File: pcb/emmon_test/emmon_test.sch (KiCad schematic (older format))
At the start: 11 parts, among them J1 Conn_01x06_Female, J2 Conn_01x08_Female, J3 Conn_01x15_Female, J4 Conn_01x15_Female, J5 Conn_01x04_Female

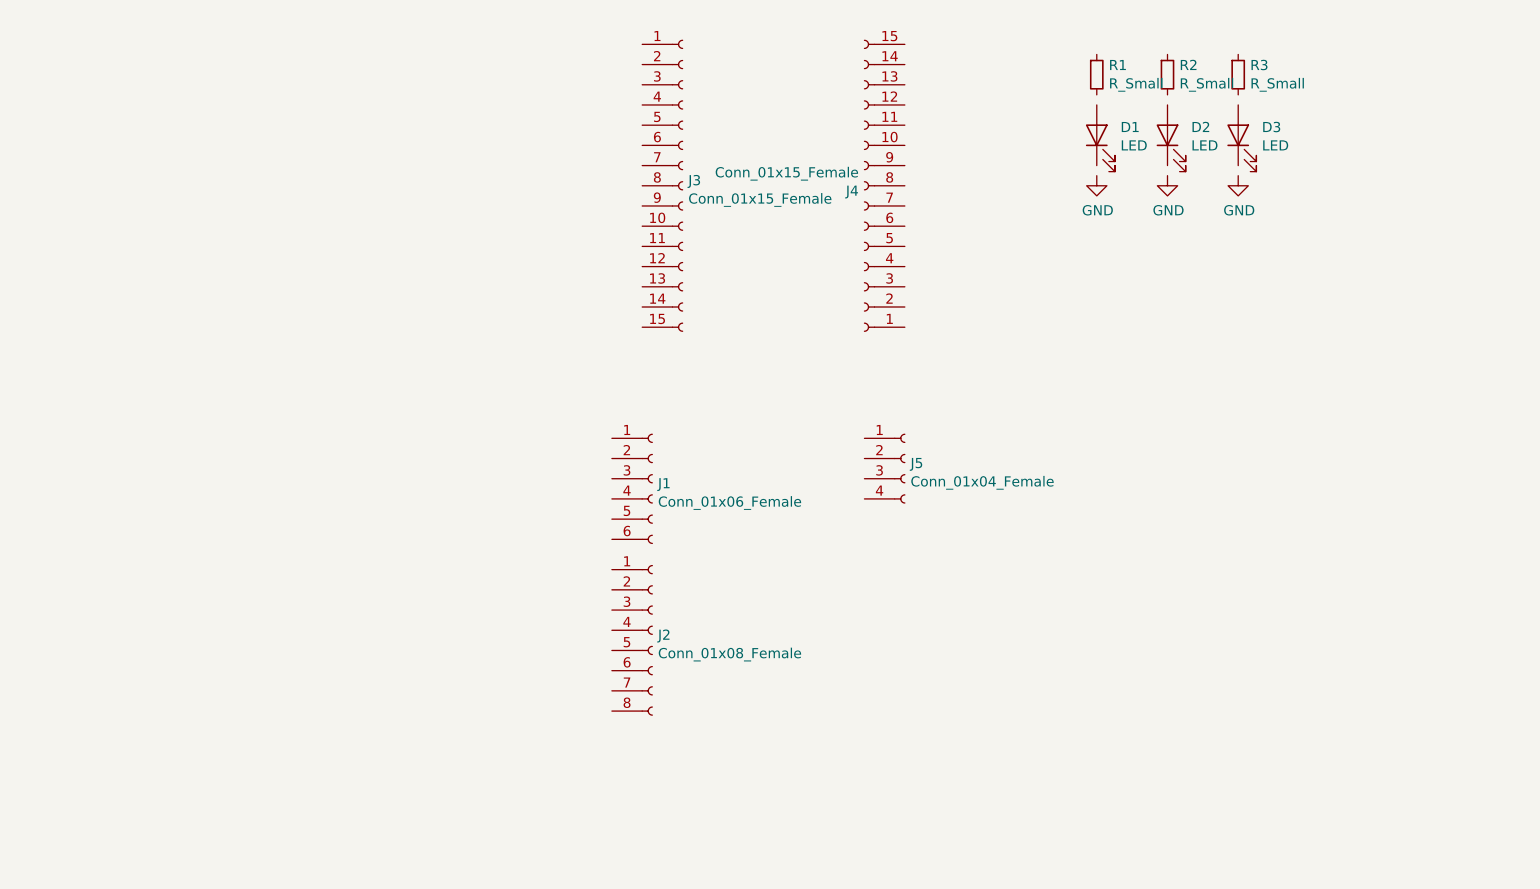
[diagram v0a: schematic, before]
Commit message: se implementa oop en el codigo y se edita el pcb
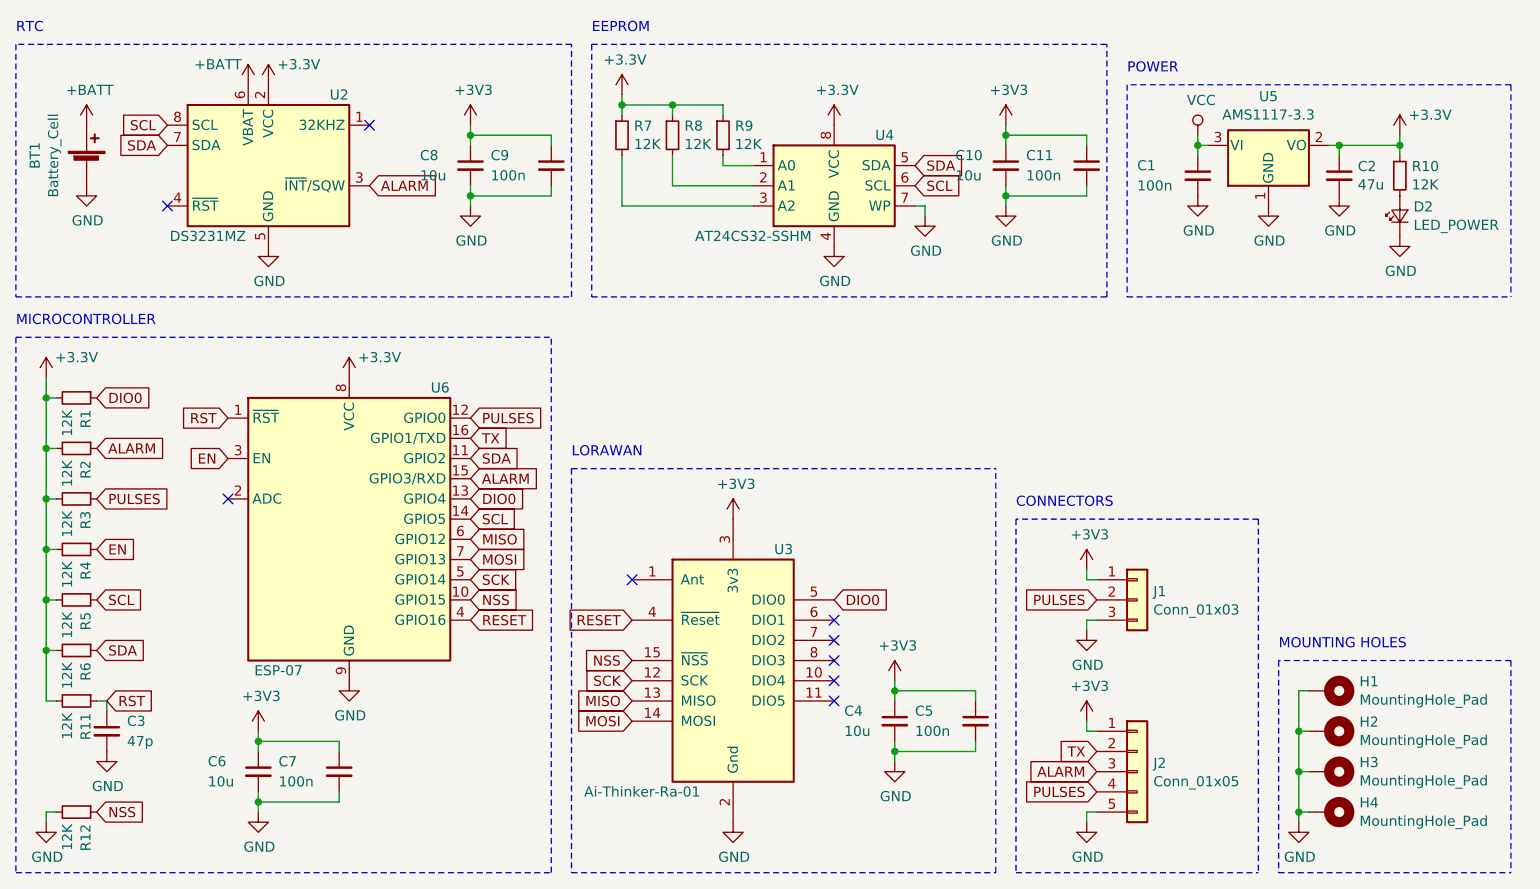
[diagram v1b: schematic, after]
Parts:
- removed D1, D2, D3: LED, LED_THT:LED_D3.0mm, symbol Device:LED
- removed J1: Conn_01x06_Female, Connector_PinSocket_2.54mm:PinSocket_1x06_P2.54mm_Vertical, symbol Connector:Conn_01x06_Female
- removed J2: Conn_01x08_Female, Connector_PinSocket_2.54mm:PinSocket_1x08_P2.54mm_Vertical, symbol Connector:Conn_01x08_Female
- removed J3, J4: Conn_01x15_Female, Connector_PinSocket_2.54mm:PinSocket_1x15_P2.54mm_Vertical, symbol Connector:Conn_01x15_Female
- removed J5: Conn_01x04_Female, Connector_PinSocket_2.54mm:PinSocket_1x04_P2.54mm_Vertical, symbol Connector:Conn_01x04_Female
- added BT1: Battery_Cell, Battery:BatteryHolder_Keystone_3002_1x2032, symbol Device:Battery_Cell
- added C1, C11, C5, C7, C9: 100n, Capacitor_SMD:C_0805_2012Metric, symbol Device:C_Small
- added C10, C4, C6, C8: 10u, Capacitor_SMD:C_0805_2012Metric, symbol Device:C_Small
- added C2: 47u, Capacitor_SMD:C_0805_2012Metric, symbol Device:C_Small
- added C3: 47p, Capacitor_SMD:C_0805_2012Metric, symbol Device:C_Small
- added D2: LED_POWER, LED_SMD:LED_0805_2012Metric, symbol Device:LED_Small
- added H1, H2, H3, H4: MountingHole_Pad, MountingHole:MountingHole_4.3mm_M4_Pad_Via, symbol Mechanical:MountingHole_Pad
- added J1: Conn_01x03, Connector_PinHeader_2.54mm:PinHeader_1x03_P2.54mm_Vertical, symbol Connector_Generic:Conn_01x03
- added J2: Conn_01x05, Connector_PinHeader_2.54mm:PinHeader_1x05_P2.54mm_Vertical, symbol Connector_Generic:Conn_01x05
- added R10, R11, R12, R4, R5, R6, R7, R8, R9: 12K, Resistor_SMD:R_0805_2012Metric, symbol Device:R_Small
- added U2: DS3231MZ, Package_SO:SOIC-8_3.9x4.9mm_P1.27mm, symbol Timer_RTC:DS3231MZ
- added U3: Ai-Thinker-Ra-01, RF_Module:Ai-Thinker-Ra-01-LoRa, symbol RF_Module:Ai-Thinker-Ra-01
- added U4: AT24CS32-SSHM, Package_SO:SOIC-8_3.9x4.9mm_P1.27mm, symbol Memory_EEPROM:AT24CS32-SSHM
- added U5: AMS1117-3.3, Package_TO_SOT_SMD:SOT-223-3_TabPin2, symbol Regulator_Linear:AMS1117-3.3
- added U6: ESP-07, RF_Module:ESP-07, symbol RF_Module:ESP-07
- R1, R2, R3: value R_Small -> 12K
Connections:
- net GND: now also BT1.2 (-), C1.2, C10.2, C11.2, C2.2, C3.2, C4.2, C5.2, C6.2, C7.2, C8.2, C9.2, D2.1 (K), H1.1, H2.1, H3.1, H4.1, J1.3 (Pin_3), J2.5 (Pin_5), R12.2, U2.5 (GND), U3.16 (Gnd), U3.2 (Gnd), U3.9 (Gnd), U4.4 (GND), U4.7 (WP), U5.1 (GND), U6.9 (GND)
- net DIO0: now reaches R1.1
- net DIO0: now also U3.5 (DIO0), U6.13 (GPIO4)
- net +3V3: now reaches R1.2
- net +3V3: now also R2.2, R3.2, C10.1, C11.1, C2.1, C4.1, C5.1, C6.1, C7.1, C8.1, C9.1, J1.1 (Pin_1), J2.1 (Pin_1), R10.1, R11.2, R4.2, R5.2, R6.2, R7.1, R8.1, R9.1, U2.2 (VCC), U3.3 (3v3), U4.8 (VCC), U5.2 (VO), U6.8 (VCC)
- net ALARM: now reaches R2.1
- net ALARM: now also J2.3 (Pin_3), U2.3 (~INT~/SQW), U6.15 (GPIO3/RXD)
- net PULSES: now reaches R3.1
- net PULSES: now also J1.2 (Pin_2), J2.4 (Pin_4), U6.12 (GPIO0)
- new net: R9.2, U4.1 (A0)
- new net: R8.2, U4.2 (A1)
- new net: R7.2, U4.3 (A2)
- new net: D2.2 (A), R10.2
- new net +BATT: BT1.1 (+), U2.6 (VBAT)
- new net EN: R4.1, U6.3 (EN)
- new net MISO: U3.13 (MISO), U6.6 (GPIO12)
- new net MOSI: U3.14 (MOSI), U6.7 (GPIO13)
- new net NSS: R12.1, U3.15 (~NSS), U6.10 (GPIO15)
- new net RESET: U3.4 (~Reset), U6.4 (GPIO16)
- new net RST: C3.1, R11.1, U6.1 (~RST)
- new net SCK: U3.12 (SCK), U6.5 (GPIO14)
- new net SCL: R5.1, U2.8 (SCL), U4.6 (SCL), U6.14 (GPIO5)
- new net SDA: R6.1, U2.7 (SDA), U4.5 (SDA), U6.11 (GPIO2)
- new net TX: J2.2 (Pin_2), U6.16 (GPIO1/TXD)
- new net VCC: C1.1, U5.3 (VI)
- no-connect marks 0 -> 9
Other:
- note added: "CONNECTORS"
- note added: "EEPROM"
- note added: "LORAWAN"
- note added: "MICROCONTROLLER"
- note added: "MOUNTING HOLES"
- note added: "POWER"
- note added: "RTC"
